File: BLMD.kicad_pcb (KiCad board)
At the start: 2 copper layers, 100 x 100 mm, 85 parts, among them J6 USB_C_Receptacle_USB2.0_14P, J8 24V IN, J9 MOTOR, Q1 RJ1G12BGN, Q2 RJ1G12BGN, Q3 RJ1G12BGN, Q4 RJ1G12BGN, Q5 RJ1G12BGN, Q6 RJ1G12BGN, SW1 NRST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

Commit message: chore: Update KiCad project files for BLMD
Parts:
- added R11: 4.7, Resistor_SMD:R_1206_3216Metric_Pad1.30x1.75mm_HandSolder, F.Cu at (248.9, 38.1)
- added R13: 1.3, Resistor_SMD:R_1206_3216Metric_Pad1.30x1.75mm_HandSolder, F.Cu at (229.9, 31.1)
- added R21: 4.7, Resistor_SMD:R_1206_3216Metric_Pad1.30x1.75mm_HandSolder, F.Cu at (231.8, 38.1)
- added R31: 4.7, Resistor_SMD:R_1206_3216Metric_Pad1.30x1.75mm_HandSolder, F.Cu at (248.9, 55.9)
- added R33: 1.3, Resistor_SMD:R_1206_3216Metric_Pad1.30x1.75mm_HandSolder, F.Cu at (229.9, 48.9)
- added R41: 4.7, Resistor_SMD:R_1206_3216Metric_Pad1.30x1.75mm_HandSolder, F.Cu at (231.8, 55.9)
- added R51: 4.7, Resistor_SMD:R_1206_3216Metric_Pad1.30x1.75mm_HandSolder, F.Cu at (248.9, 73.7)
- added R53: 1.3, Resistor_SMD:R_1206_3216Metric_Pad1.30x1.75mm_HandSolder, F.Cu at (229.9, 66.7)
- added R61: 4.7, Resistor_SMD:R_1206_3216Metric_Pad1.30x1.75mm_HandSolder, F.Cu at (231.8, 73.7)
- C2, C3, C4, C5, D11, D21, D31, D41, D51, D61, U11: moved to B.Cu
- moved R24 123.9 mm to (205.7, 38.7)
- moved R34 119.2 mm to (205.7, 51.4)
- moved R14 110.4 mm to (205.7, 33.7), turned to 0 degrees
- moved R1 108.3 mm to (198.1, 1.91)
- moved R2 106.8 mm to (198.1, 6.35)
- moved R44 105.7 mm to (205.7, 56.5)
- moved R54 102.0 mm to (205.7, 69.2)
- moved R64 102.0 mm to (205.7, 74.3)
- moved C63 101.1 mm to (207.6, 80.0), turned to -90 degrees
- moved C1 96.9 mm to (191.8, 5.08)
- moved C8 79.7 mm to (254.0, 30.5)
- moved C43 77.1 mm to (207.6, 62.2), turned to -90 degrees
- moved C23 73.5 mm to (207.6, 44.5), turned to -90 degrees
- moved C5 71.9 mm to (191.1, 55.9)
- moved C4 71.7 mm to (191.1, 54.0)
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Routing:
- net Net-(D51-K): track 0.00 -> 34.9 mm, vias 0 -> 2
- net Net-(D11-K): track 0.00 -> 34.9 mm, vias 0 -> 2
- net Net-(D31-K): track 0.00 -> 34.9 mm, vias 0 -> 2
- net /Inverter/W: track 43.3 -> 77.0 mm, vias 0 -> 3
- net /Inverter/U: track 44.6 -> 77.0 mm, vias 0 -> 3
- net /Inverter/V: track 35.2 -> 66.9 mm, vias 0 -> 3
- net +12V: track 70.6 -> 96.0 mm, vias 3 -> 4
- net Net-(D11-A): track 24.2 -> 4.81 mm, vias 0 -> 1
- net Net-(D51-A): track 23.4 -> 4.81 mm, vias 0 -> 1
- net +24V: track 59.5 -> 77.5 mm, vias 0 -> 4
- net Net-(D31-A): track 22.7 -> 4.81 mm, vias 0 -> 1
- net Net-(D22-A): track 12.7 -> 28.0 mm, vias 0 -> 1
- net GNDPWR: track 71.6 -> 86.9 mm, vias 0 -> 3
- net Net-(D41-K): track 0.00 -> 15.2 mm, vias 0 -> 2
- net Net-(D21-K): track 0.00 -> 15.2 mm, vias 0 -> 2
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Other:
- board text removed: "+"
- board text removed: "-"

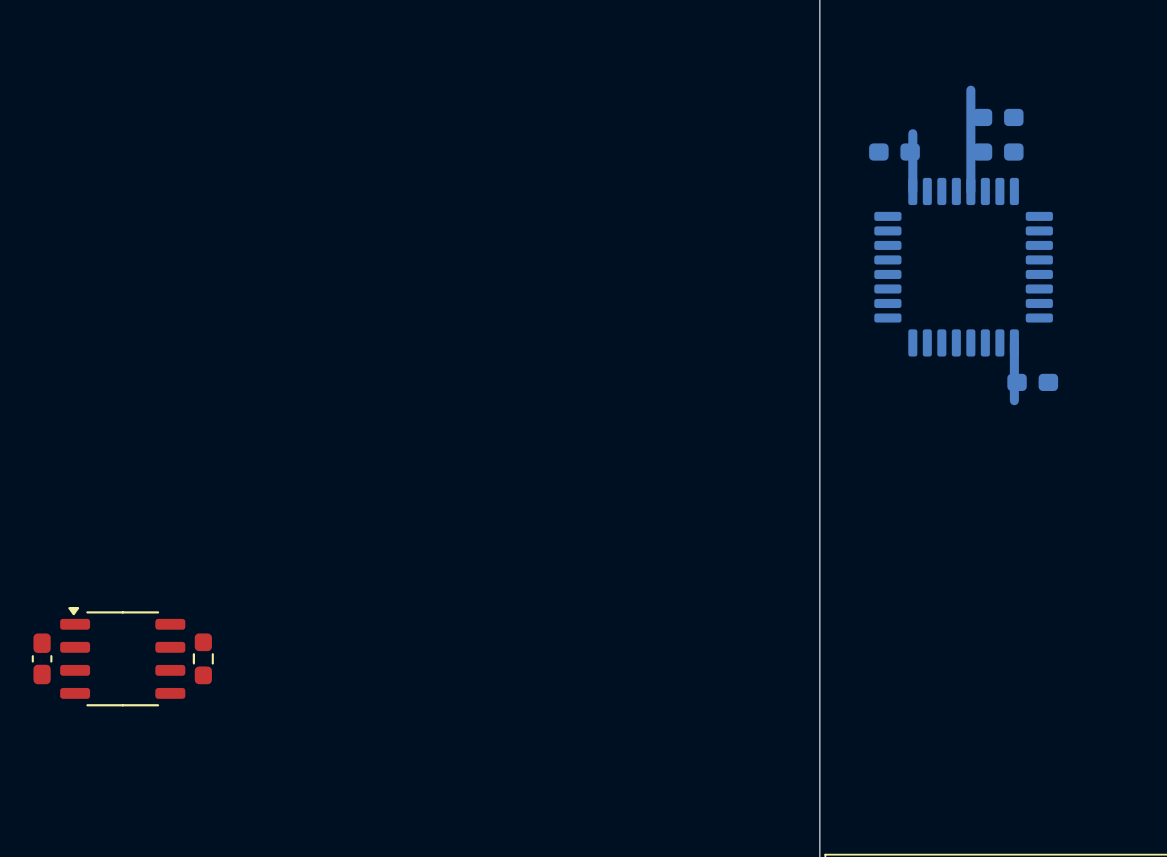
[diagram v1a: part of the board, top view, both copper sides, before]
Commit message: feat: Add symbols for BD41044FJ-C and NJM12877
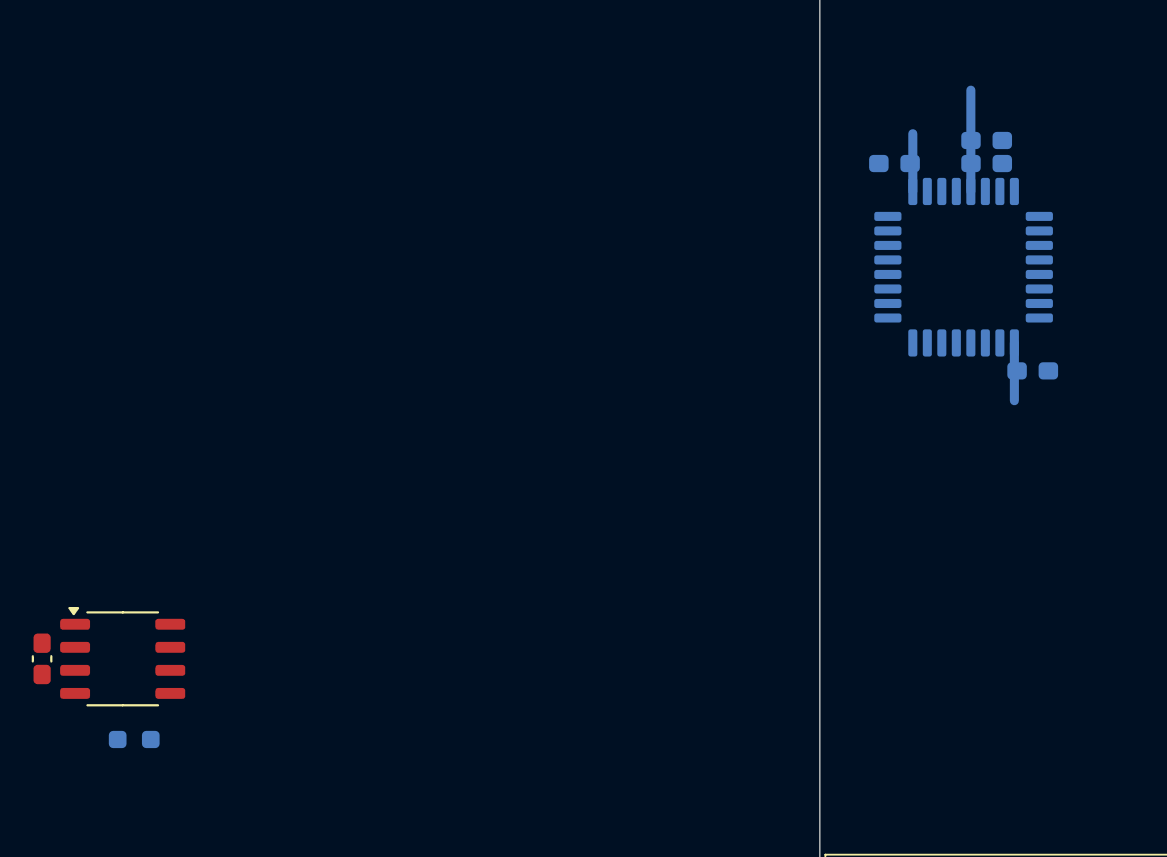
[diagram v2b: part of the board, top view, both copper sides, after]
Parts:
- R7: moved to B.Cu
- moved R7 5.85 mm to (143.5, 88.3), turned to 0 degrees
- moved C4 1.42 mm to (190.5, 55.2)
- moved C5 0.90 mm to (190.5, 56.5)
- moved C3 0.64 mm to (193.0, 67.9)
- moved C2 0.63 mm to (185.4, 56.5)

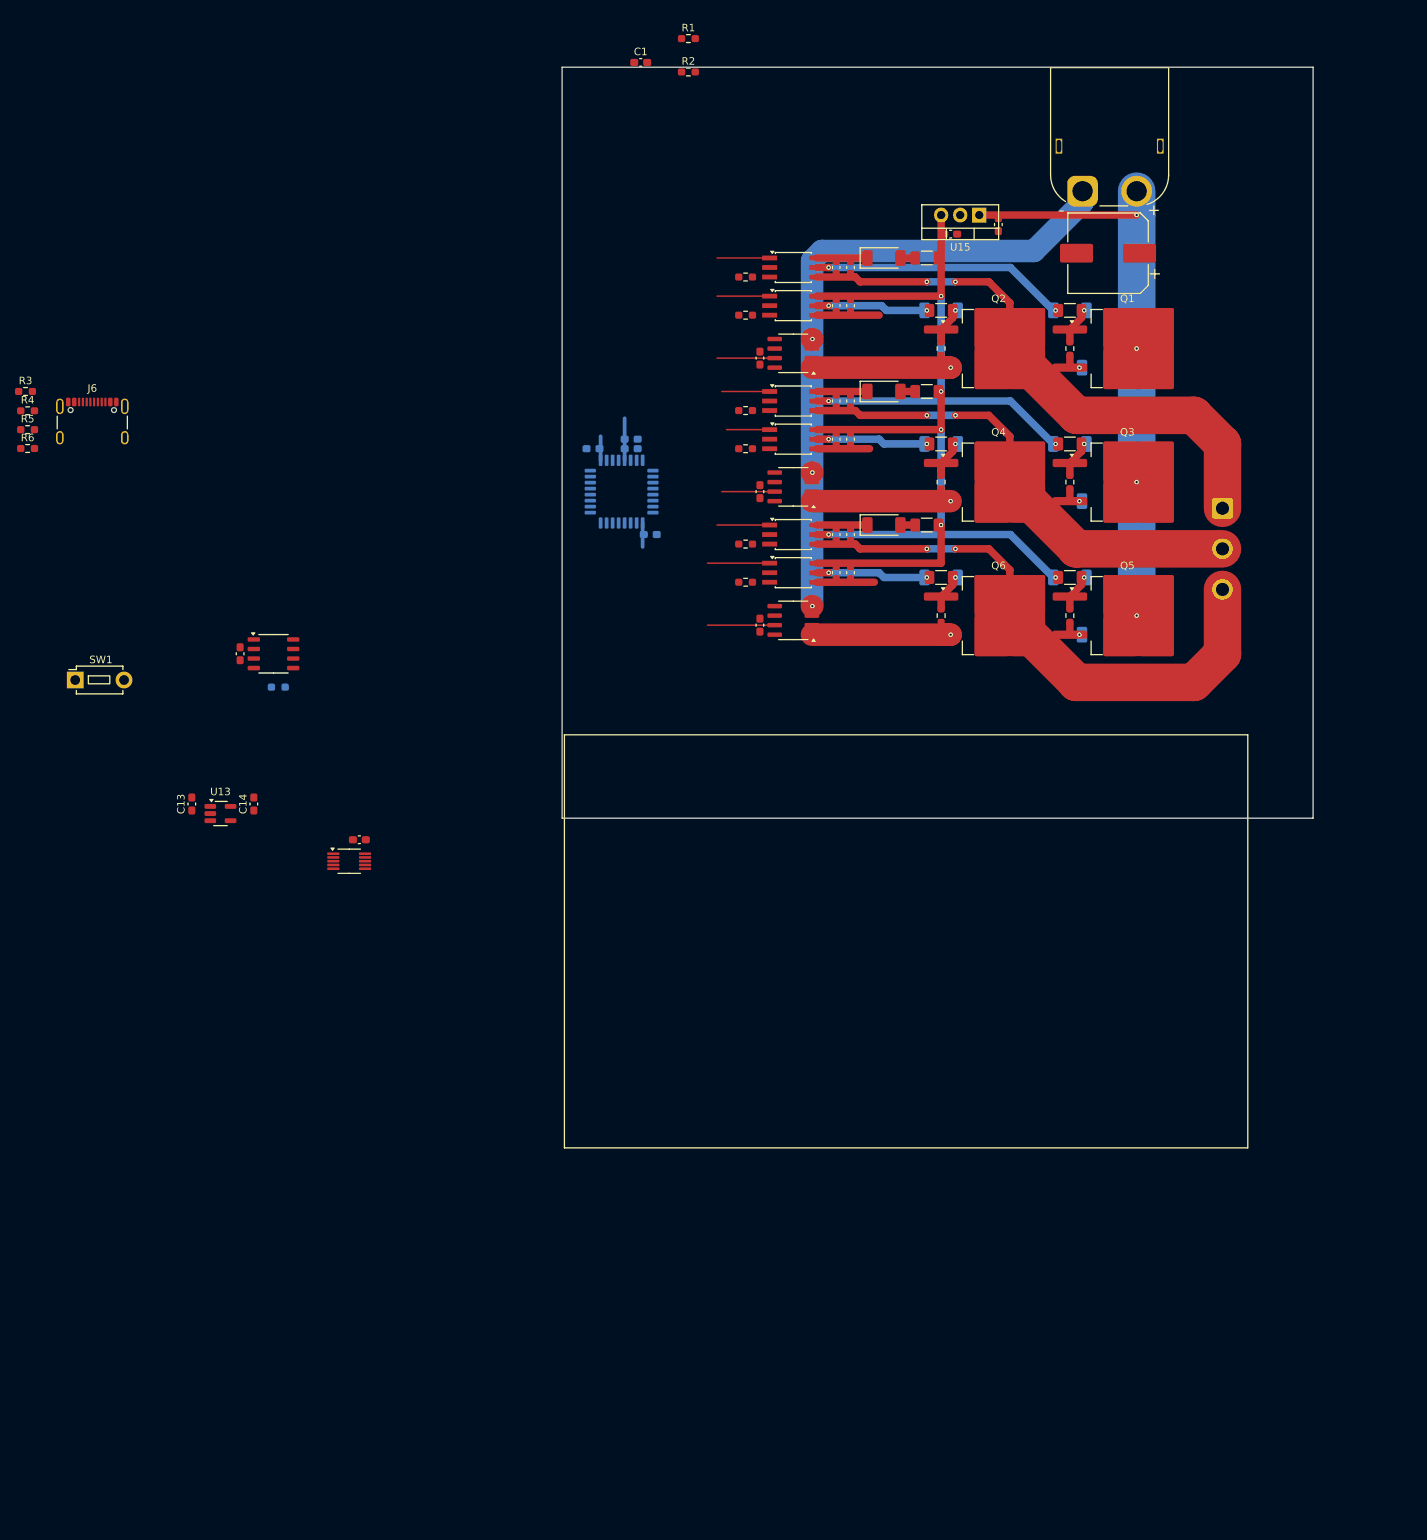
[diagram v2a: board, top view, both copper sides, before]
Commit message: chore: Exclude power pin not driven errors in ERC
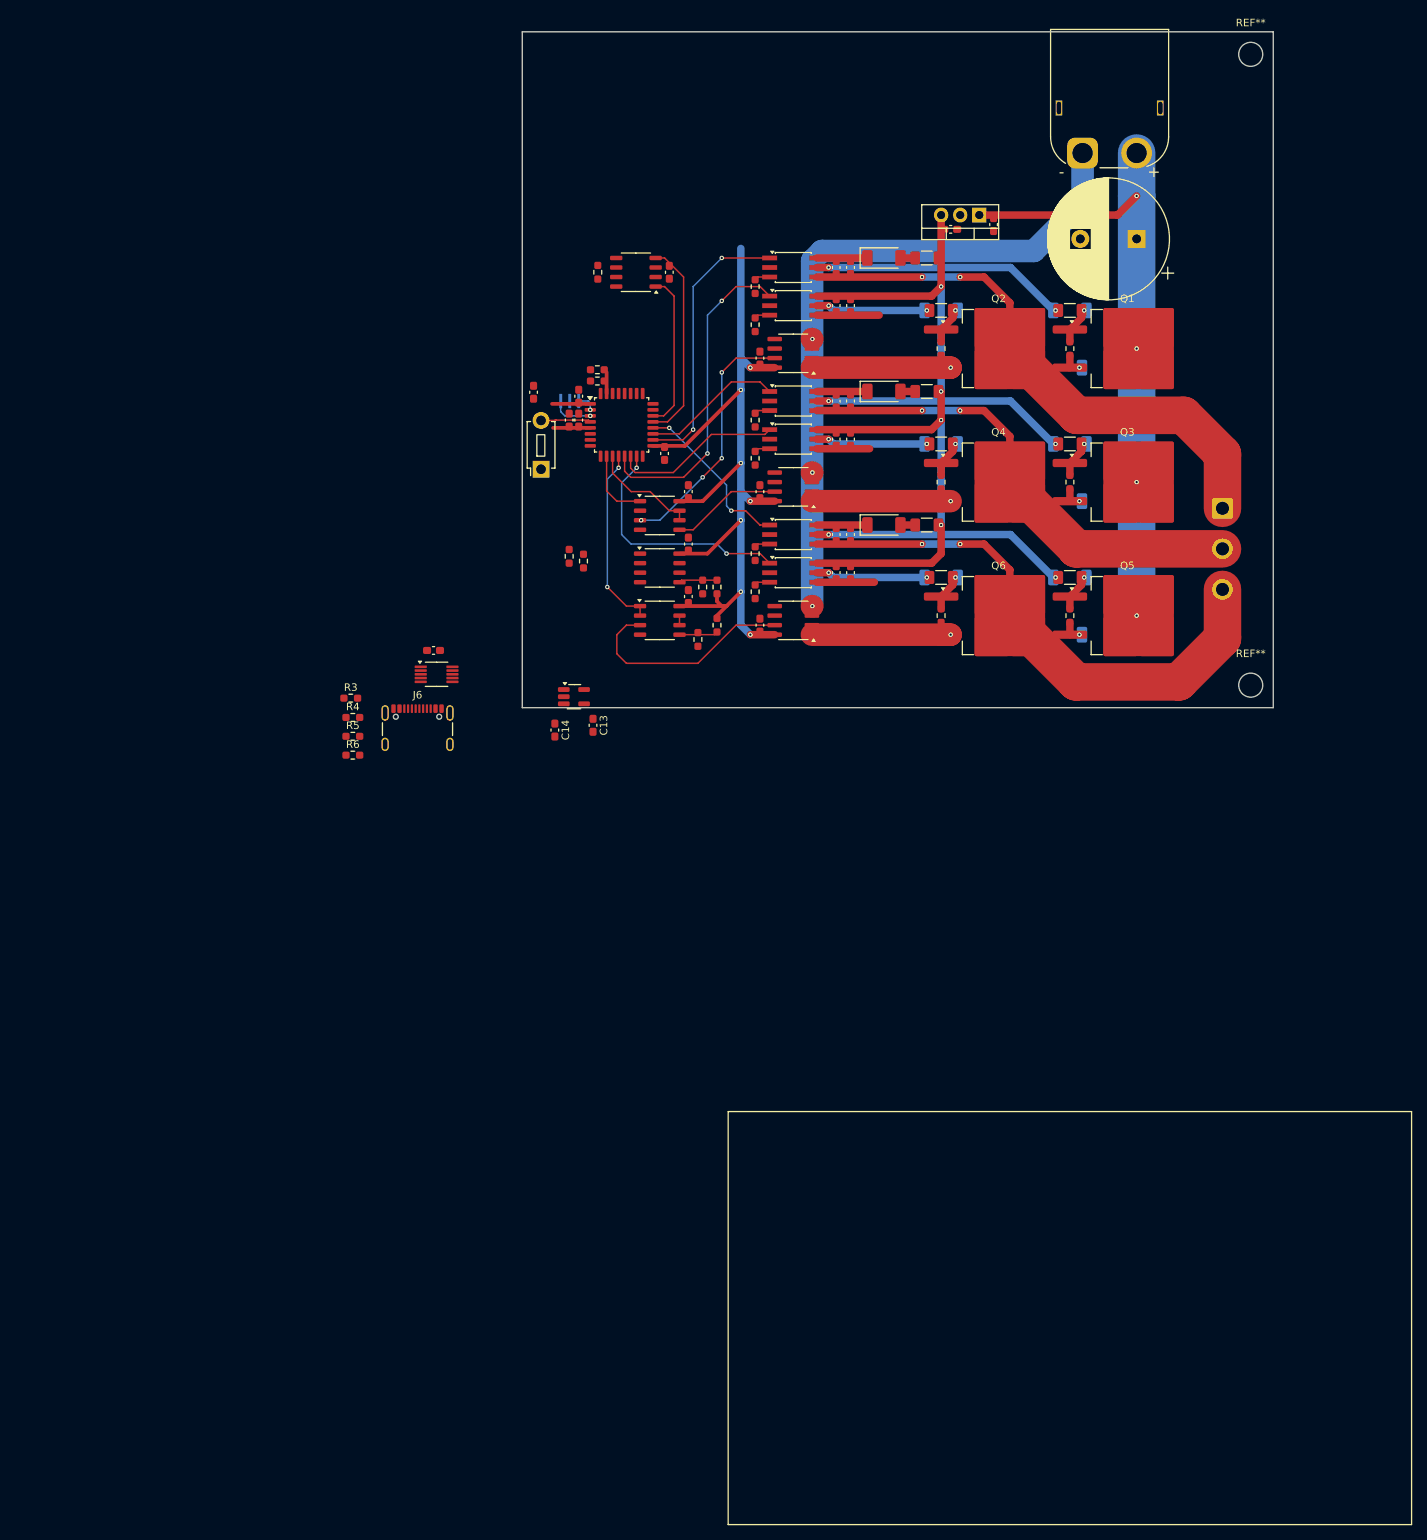
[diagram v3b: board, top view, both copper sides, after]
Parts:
- added C17: 0.1u, Capacitor_SMD:C_0603_1608Metric_Pad1.08x0.95mm_HandSolder, F.Cu at (198.1, 62.2)
- added C18: 0.1u, Capacitor_SMD:C_0603_1608Metric_Pad1.08x0.95mm_HandSolder, F.Cu at (198.1, 76.2)
- added C19: 0.1u, Capacitor_SMD:C_0603_1608Metric_Pad1.08x0.95mm_HandSolder, F.Cu at (198.1, 69.2)
- added R15: 10k, Resistor_SMD:R_0603_1608Metric_Pad0.98x0.95mm_HandSolder, F.Cu at (201.9, 80.0)
- added R16: 10k, Resistor_SMD:R_0603_1608Metric_Pad0.98x0.95mm_HandSolder, F.Cu at (199.4, 81.9)
- added R17: 10k (DNP), Resistor_SMD:R_0603_1608Metric_Pad0.98x0.95mm_HandSolder, F.Cu at (182.2, 70.8)
- added R18: 10k (DNP), Resistor_SMD:R_0603_1608Metric_Pad0.98x0.95mm_HandSolder, F.Cu at (184.2, 71.5)
- added R19: 10k (DNP), Resistor_SMD:R_0603_1608Metric_Pad0.98x0.95mm_HandSolder, F.Cu at (201.9, 74.9)
- added R20: 10k (DNP), Resistor_SMD:R_0603_1608Metric_Pad0.98x0.95mm_HandSolder, F.Cu at (200.0, 74.9)
- added REF**: MountingHole_3.2mm_M3, MountingHole:MountingHole_3.2mm_M3, F.Cu at (273.0, 88.0)
- added REF**: MountingHole_3.2mm_M3, MountingHole:MountingHole_3.2mm_M3, F.Cu at (273.0, 4.00)
- added U16: NJU77552G, Package_SO:SOP-8_3.9x4.9mm_P1.27mm, F.Cu at (194.3, 65.4)
- added U17: NJU77552G, Package_SO:SOP-8_3.9x4.9mm_P1.27mm, F.Cu at (194.3, 79.4)
- added U18: NJU77552G, Package_SO:SOP-8_3.9x4.9mm_P1.27mm, F.Cu at (194.3, 72.4)
- added Y1: 16MHz, Crystal:Resonator_SMD_Murata_CSTxExxV-3Pin_3.0x1.1mm, B.Cu at (182.3, 50.2)
- C2, C3, C4, C5, R7, U11: moved to F.Cu
- C8: value 330u -> 1000u; footprint Capacitor_SMD:CP_Elec_10x10.5 -> Capacitor_THT:CP_Radial_D16.0mm_P7.50mm
- moved C7 76.5 mm to (195.6, 33.0), turned to 90 degrees
- moved U12 70.1 mm to (191.1, 33.0), turned to 180 degrees
- moved R7 69.7 mm to (186.1, 33.0), turned to 90 degrees
- moved SW1 68.1 mm to (178.5, 59.2), turned to 90 degrees
- moved J6 59.5 mm to (162.1, 94.8)
- moved R4 59.5 mm to (153.4, 92.3)
- moved R5 59.5 mm to (153.4, 94.8)
- moved R6 59.5 mm to (153.4, 97.3)
- moved R3 59.5 mm to (153.2, 89.7)
- moved C13 54.4 mm to (185.4, 93.3), turned to -90 degrees
- moved U13 49.6 mm to (182.9, 89.5)
- moved C1 46.2 mm to (177.5, 49.0), turned to 90 degrees
- moved R1 45.7 mm to (186.0, 46.0)
- moved R2 42.9 mm to (186.0, 47.5), turned to 180 degrees
- moved C14 41.3 mm to (180.3, 94.0), turned to -90 degrees
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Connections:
- net /CAN_RX renamed /MCU/CAN_RX
- net /CAN_TX renamed /MCU/CAN_TX
- net /ENCODER_A renamed /MCU/ENCODER_A
- net /ENCODER_B renamed /MCU/ENCODER_B
- net /NRST renamed /MCU/NRST
- net /PWMUH renamed /Inverter/PWMUH
- net /PWMUL renamed /Inverter/PWMUL
- net /PWMVH renamed /Inverter/PWMVH
- net /PWMVL renamed /Inverter/PWMVL
- net /PWMWH renamed /Inverter/PWMWH
- net /PWMWL renamed /Inverter/PWMWL
- net /SWCLK renamed /MCU/SWCLK
- net /SWDIO renamed /MCU/SWDIO
- net /SWO renamed /MCU/SWO
- net /USART1_RX renamed /MCU/HALLW
- net /USART1_TX renamed /MCU/HALLV
- net /USART2_RX renamed /MCU/USART2_RX
- net /USART2_TX renamed /MCU/USART2_TX
- U11 pad 10: /IU -> /MCU/IU
- U11 pad 11: /IV -> /MCU/IV
- U11 pad 12: /IW -> /MCU/IW
- U11 pad 2: unconnected-(U11-PF0-Pad2) -> Net-(U11-PF0)
- U11 pad 25: unconnected-(U11-PA15-Pad25) -> /MCU/HALLU
- U11 pad 3: unconnected-(U11-PF1-Pad3) -> Net-(U11-PF1)
- U11 pad 6: /ADC1_IN1 -> /MCU/ADC1_IN1
- U11 pad 7: /ADC1_IN2 -> /MCU/ADC1_IN2
- U7 pad 7: /IU -> /Inverter/IU
- U8 pad 7: /IV -> /Inverter/IV
- U9 pad 7: /IW -> /Inverter/IW
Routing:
- net +3V3: track 12.0 -> 124.0 mm, vias 0 -> 7
- net /Inverter/PWMUL: track 7.01 -> 43.5 mm, vias 0 -> 2
- net /Inverter/IU: track 0.00 -> 33.4 mm, vias 0 -> 4
- net /Inverter/IW: track 0.00 -> 29.8 mm
- net /Inverter/PWMUH: track 7.01 -> 36.7 mm, vias 0 -> 2
- net /MCU/CAN_RX: track 0.00 -> 26.9 mm
- net /MCU/IW: track 0.00 -> 24.9 mm, vias 0 -> 2
- net /Inverter/PWMWL: track 8.28 -> 32.5 mm, vias 0 -> 2
- net /MCU/CAN_TX: track 0.00 -> 20.9 mm
- net /Inverter/PWMVL: track 5.74 -> 22.7 mm
- net /Inverter/PWMWH: track 7.01 -> 22.5 mm, vias 0 -> 2
- net /Inverter/IV: track 0.00 -> 14.8 mm
- net /MCU/IV: track 0.00 -> 14.5 mm
- net /Inverter/PWMVH: track 6.38 -> 18.9 mm
- net /MCU/IU: track 0.00 -> 9.64 mm
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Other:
- board size 100 x 100 mm -> 100 x 90 mm
